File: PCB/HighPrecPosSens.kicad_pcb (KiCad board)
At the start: 2 copper layers, 60 x 75 mm, 81 parts, among them J1 Conn_01x02_Male, J2 Conn_01x02_Male, J3 Conn_01x02_Male, J4 Conn_01x02_Male, J5 Conn_01x06_Male, U1 ST1S14PHR, U2 S12443, U3 LM393DR2G, U4 LM393DR2G, U5 74LVC541A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

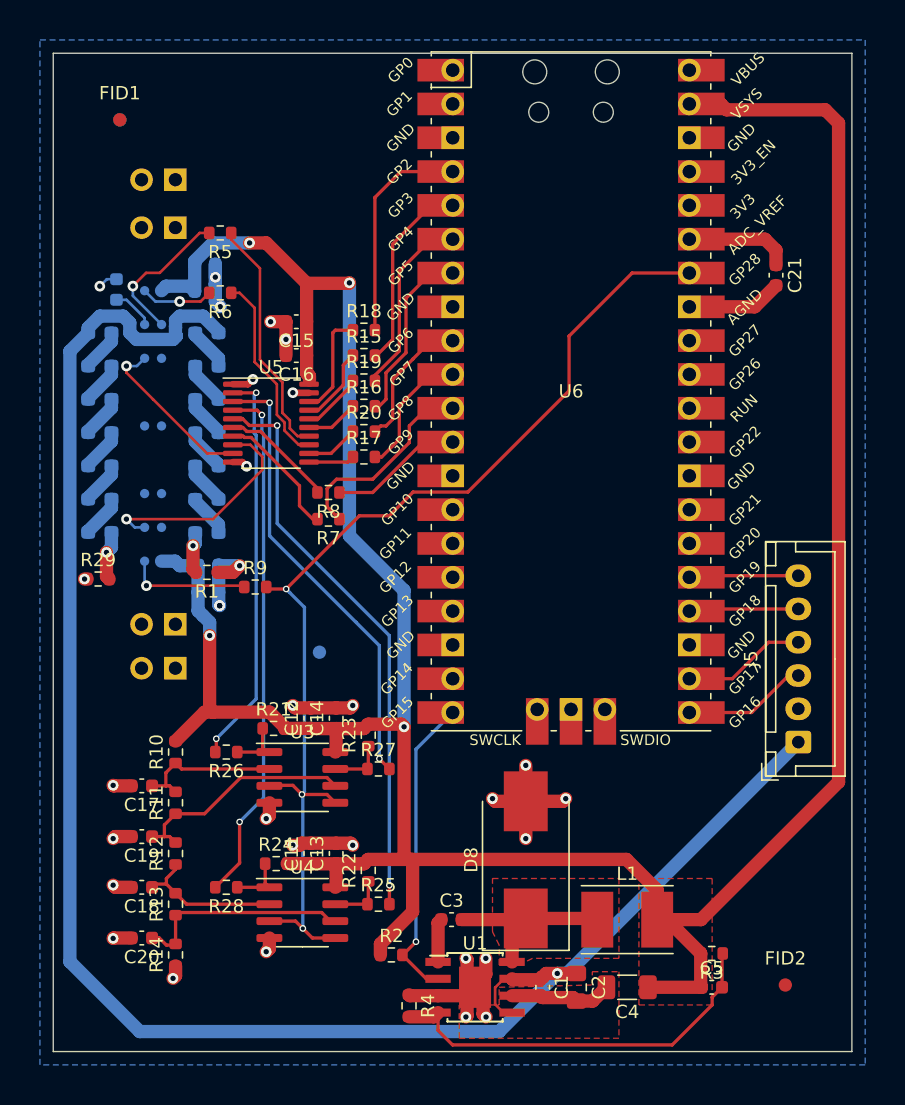
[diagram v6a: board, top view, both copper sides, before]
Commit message: some mounting holes added
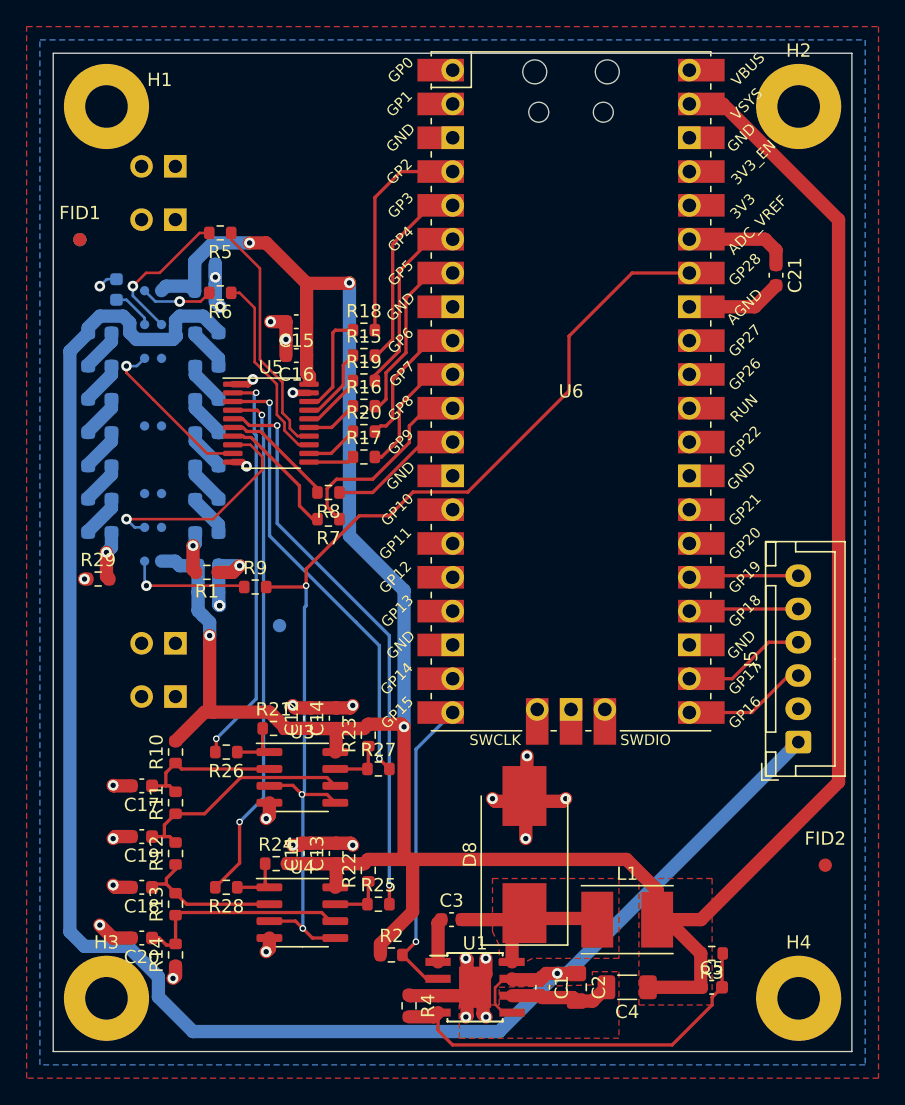
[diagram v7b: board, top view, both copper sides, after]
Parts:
- added H1: MountingHole_Pad, MountingHole:MountingHole_3.2mm_M3_Pad, F.Cu at (34.0, 74.0)
- added H2: MountingHole_Pad, MountingHole:MountingHole_3.2mm_M3_Pad, F.Cu at (86.0, 74.0)
- added H3: MountingHole_Pad, MountingHole:MountingHole_3.2mm_M3_Pad, F.Cu at (34.0, 141.0)
- added H4: MountingHole_Pad, MountingHole:MountingHole_3.2mm_M3_Pad, F.Cu at (86.0, 141.0)
- moved FID1 9.49 mm to (32.0, 84.0)
- moved FID2 9.49 mm to (88.0, 131.0)
- moved FID4 9.49 mm to (32.0, 84.0)
- moved FID3 3.61 mm to (47.0, 113.0)
- moved J3 2.13 mm to (39.2, 118.3)
- moved J1 1.43 mm to (39.2, 114.3)
- moved J2 1.00 mm to (39.2, 78.5)
- moved J4 0.60 mm to (39.2, 82.5)
- moved D8 0.41 mm to (65.4, 130.2)
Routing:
- net +3.3V: track 237.2 -> 233.0 mm
- net GND: track 76.8 -> 78.9 mm

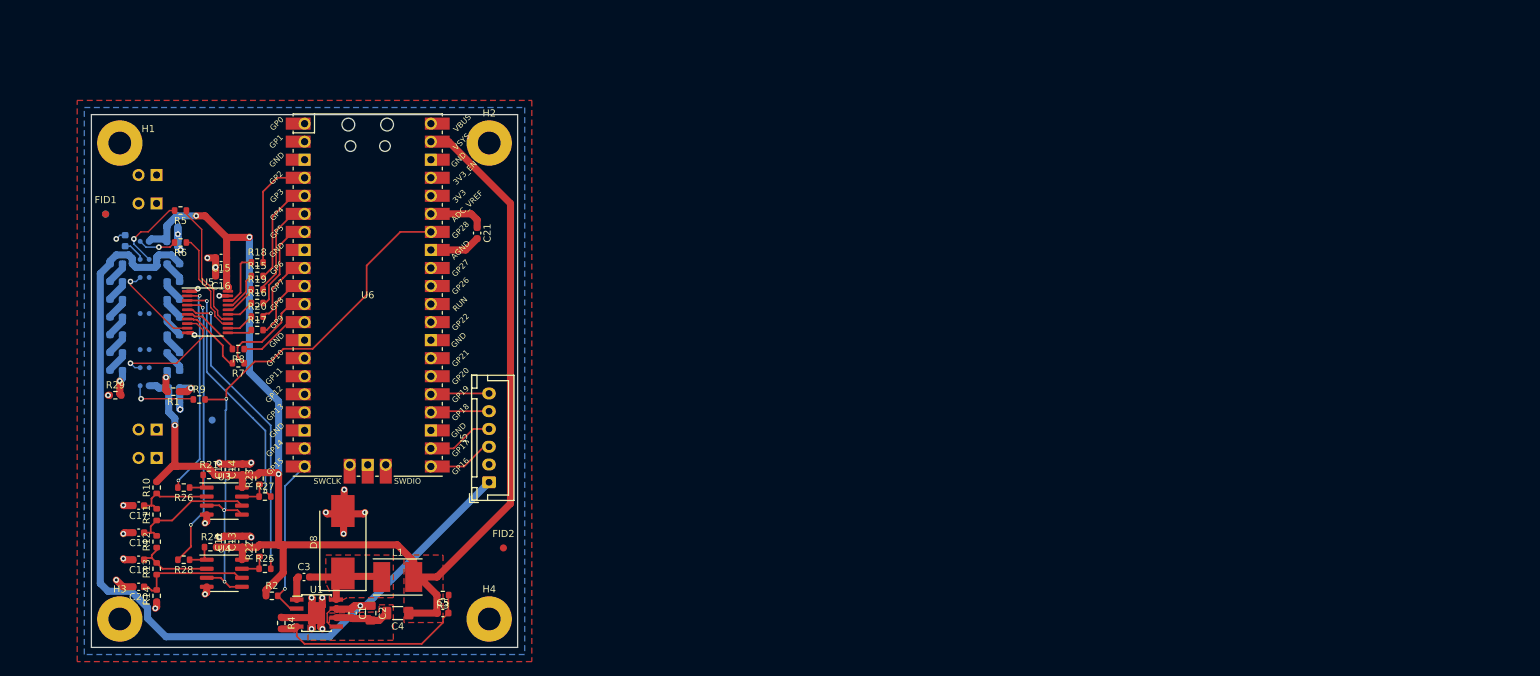
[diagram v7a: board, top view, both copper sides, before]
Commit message: Some readibility and overlap issues fixed, added some more ground vias
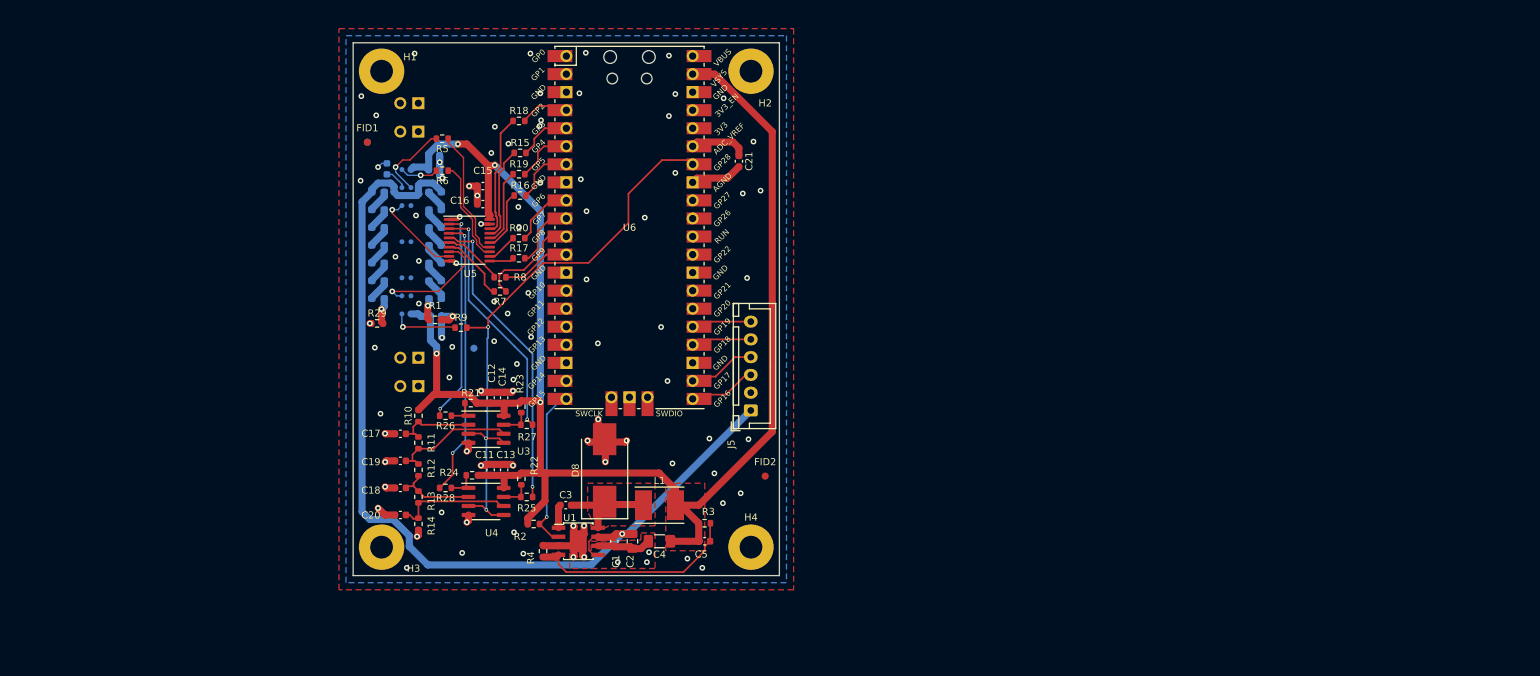
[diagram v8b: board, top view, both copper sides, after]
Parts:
- moved R18 41.9 mm to (90.2, 70.9)
- moved R15 40.9 mm to (90.3, 75.4)
- moved R19 40.3 mm to (90.2, 78.4)
- moved R16 40.0 mm to (90.3, 81.4)
- moved R20 38.5 mm to (90.2, 87.4)
- moved R13 38.2 mm to (76.0, 123.8)
- moved R14 38.2 mm to (76.0, 127.6)
- moved C1 38.2 mm to (103.6, 130.1)
- moved C21 38.2 mm to (121.2, 76.6)
- moved C3 38.2 mm to (96.8, 125.0)
- moved J2 38.2 mm to (76.0, 68.4)
- moved J4 38.2 mm to (76.0, 72.4)
- moved J5 38.2 mm to (122.8, 111.6)
- moved R10 38.2 mm to (76.0, 112.4)
- moved R11 38.2 mm to (76.0, 116.2)
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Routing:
- net Net-(R18-Pad2): track 16.6 -> 7.06 mm
- net Net-(R18-Pad1): track 7.90 -> 17.2 mm
- net Net-(R15-Pad1): track 5.87 -> 13.3 mm
- net Net-(R15-Pad2): track 14.7 -> 7.61 mm
- net Net-(R19-Pad1): track 4.62 -> 10.8 mm
- net Net-(R19-Pad2): track 14.0 -> 8.19 mm
- net Net-(R16-Pad2): track 13.6 -> 8.57 mm
- net Net-(R16-Pad1): track 3.96 -> 8.56 mm
- net +3.3V: track 233.0 -> 231.4 mm
- net Net-(R20-Pad2): track 10.4 -> 9.03 mm
- net GND: vias 31 -> 93
